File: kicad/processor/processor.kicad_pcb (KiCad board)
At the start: 4 copper layers, 75 x 50 mm, 95 parts, among them J101 CONN_02X07, J201 V_QI, J202 GND, J203 Battery, M401 MICROSD, Q201 DMG3415U, Q202 DMG3415U, Q203 DMG3414U, Q204 DMG3415U, Q205 DMG3415U, Q301 DMG3415U, Q401 DMG3415U, Q501 MMBT4401, Q502 MMBT4401, SW201 SW, SW501 SWITCH_PUSHBUTTON, SW502 SWITCH_PUSHBUTTON, U101 ESP32-WROOM, U102 BME280, U103 TCA9534A, U201 MCP73832, U202 NCP694-3.3, U301 FGPMMOPA6H, U501 USB_B_Socket, U502 SP3003-04, U503 CP2102N

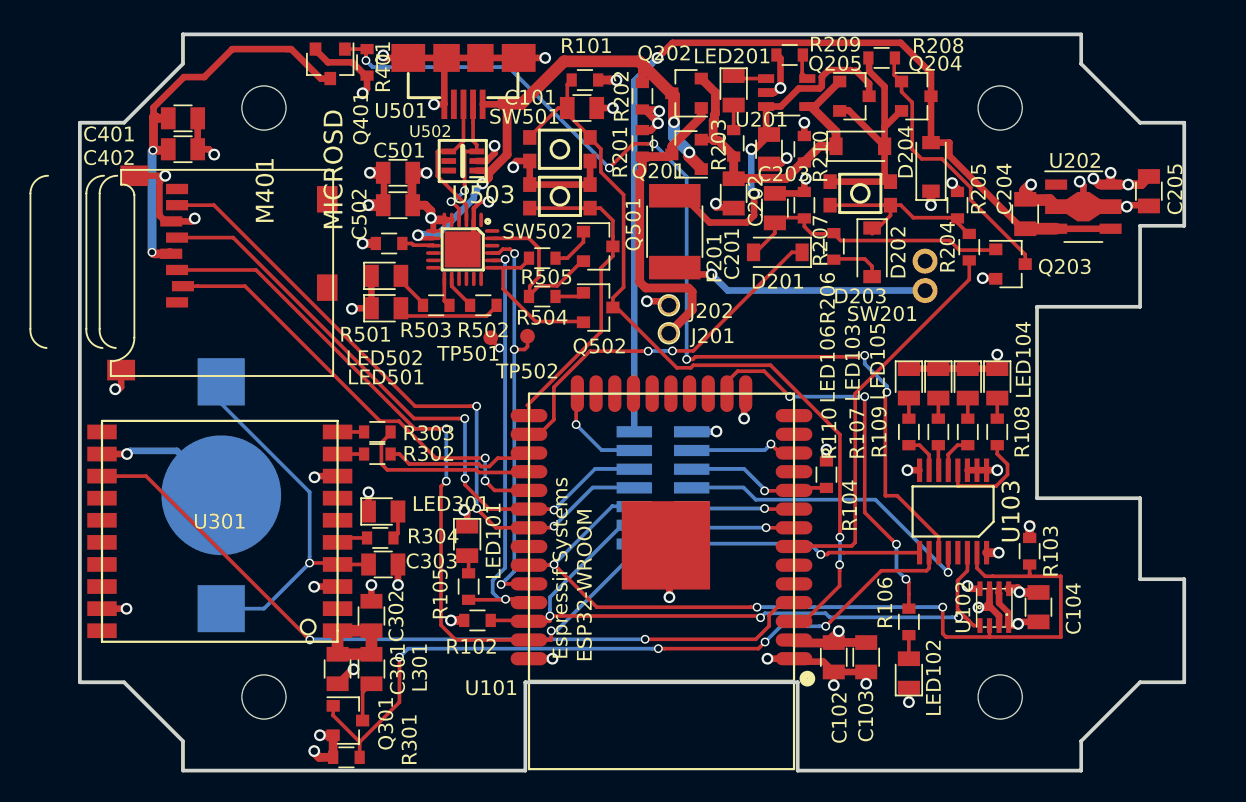
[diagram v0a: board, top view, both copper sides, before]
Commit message: Split analog SPI to be separate from SD pins, USB bus powered, added caps, updated todo, more
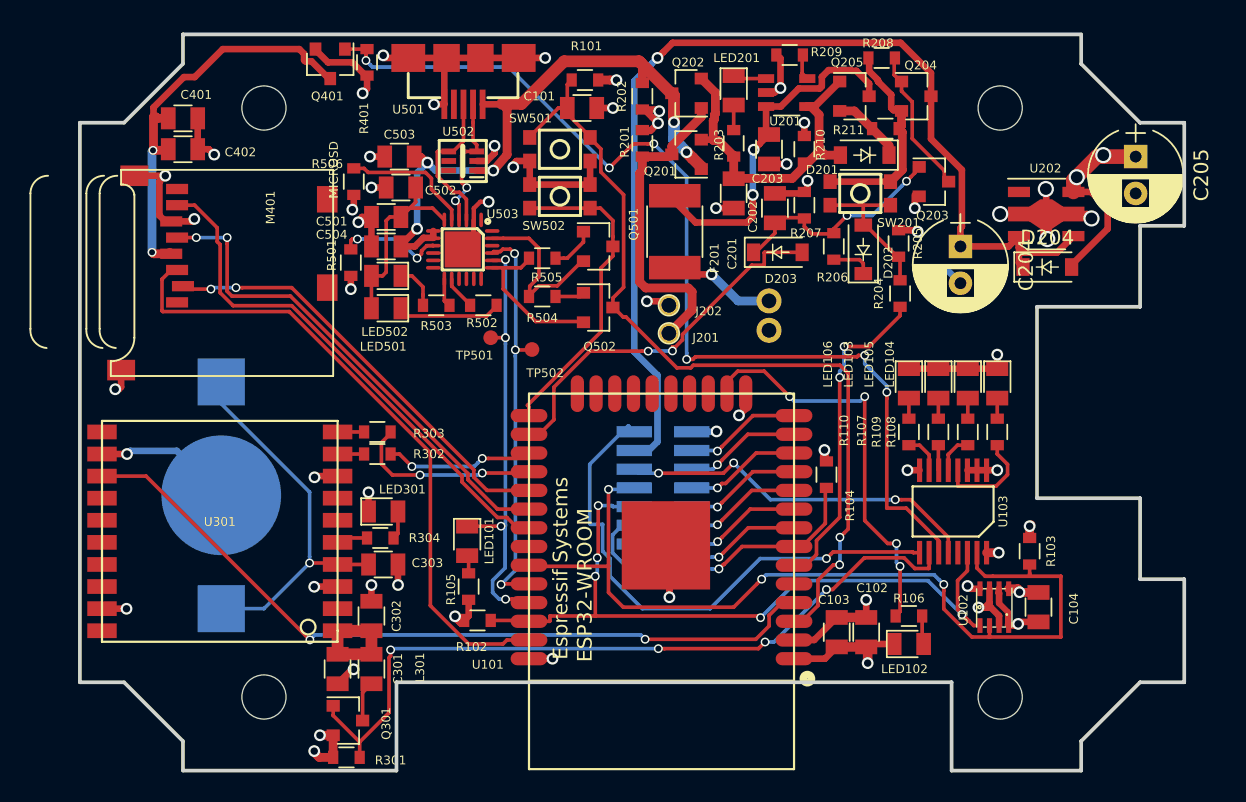
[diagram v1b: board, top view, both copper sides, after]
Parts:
- added C503: 4.7uF, paddle:SMD_0805, F.Cu at (21.7, 8.30)
- added C504: 0.1uF, paddle:SMD_0805, F.Cu at (20.8, 14.4)
- added R211: 1R0, paddle:R_0603, F.Cu at (54.7, 6.40)
- added R506: 1k, paddle:R_0603, F.Cu at (18.6, 10.0)
- C204, C205: value 10uF -> 100uF/10V; footprint paddle:SMD_0805 -> Capacitors_THT:CP_Radial_D6.3mm_P2.50mm
- C501: value 10uF -> 4.7uF
- D201, D203, D204: value SS24FL -> Schottky
- R107, R110: value 330 -> 220
- R205: value 1Meg -> 100k
- moved J203 10.9 mm to (46.8, 19.1), turned to 270 degrees
- moved D204 10.4 mm to (65.7, 15.8), turned to 0 degrees
- moved D203 9.12 mm to (47.4, 14.8)
- moved D201 8.85 mm to (53.3, 8.20)
- moved Q203 7.64 mm to (58.0, 10.0)
- moved R204 5.66 mm to (55.7, 17.6)
- moved C204 4.92 mm to (59.8, 14.4), turned to 270 degrees
- moved R205 4.77 mm to (55.6, 14.2)
- moved C501 3.10 mm to (20.8, 12.4)
- moved R501 2.91 mm to (18.4, 15.5), turned to 270 degrees
- moved C102 2.78 mm to (53.4, 40.6)
- moved C103 2.62 mm to (51.4, 40.6)
- moved U202 2.57 mm to (65.6, 12.2)
- moved C205 2.52 mm to (71.7, 8.30)
- moved LED102 2.00 mm to (56.3, 41.4), turned to 0 degrees
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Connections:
- C501 pad 1: +3V3 -> Net-(C501-Pad1)
- C502 pad 1: +3V3 -> Net-(C501-Pad1)
- D201 pad 1: /KEEPALIVE -> Net-(D201-Pad1)
- D201 pad 2: Net-(C202-Pad1) -> /power/V+EXT
- D203 pad 1: /power/V+EXT -> Net-(C202-Pad1)
- D203 pad 2: /power/V_UNREG -> /KEEPALIVE
- D204 pad 1: +3V3 -> /+V_UNREG_SW
- D204 pad 2: /+V_UNREG_SW -> +3V3
- J101 pad 1: /SPI_SDO -> /AN3_CS*
- J101 pad 10: /BUSY* -> /SPI_MISO
- J101 pad 11: /AN3_CS* -> /+V_UNREG_SW
- J101 pad 12: /AN0_CS* -> /SPI_SCLK
- J101 pad 13: /+V_UNREG_SW -> /+3.3VA_ENABLE
- J101 pad 2: /+3.3VA_ENABLE -> /AN2_CS*
- J101 pad 3: /I2C_SCK -> /PIO_B_BUSY*
- J101 pad 5: /I2C_SDA -> /I2C_SCK
- J101 pad 6: /AN2_CS* -> /AN0_CS*
- J101 pad 7: /SPI_SDI -> /I2C_SDA
- J101 pad 8: /AN_REFSEL -> /SPI_MOSI
- J101 pad 9: /SPI_SCLK -> /PIO_A
- LED101 pad 1: GND -> /CON_TXD
- LED501 pad 1: GND -> Net-(LED501-Pad1)
- LED501 pad 2: Net-(LED501-Pad2) -> Net-(C501-Pad1)
- LED502 pad 1: GND -> Net-(LED502-Pad1)
- LED502 pad 2: Net-(LED502-Pad2) -> Net-(C501-Pad1)
- M401 pad 1: Net-(M401-Pad1) -> (no net)
- M401 pad 3: /SPI_SDO -> /SD_MOSI
- M401 pad 5: /SPI_SCLK -> /SD_SCLK
- M401 pad 7: /SPI_SDI -> /SD_MISO
- M401 pad 8: Net-(M401-Pad8) -> (no net)
- M401 pad CD1: Net-(M401-PadCD1) -> (no net)
- M401 pad CD2: Net-(M401-PadCD2) -> (no net)
- Q205 pad 2: /power/V_UNREG -> Net-(D201-Pad1)
- R104 pad 2: /BUSY* -> /PIO_B_BUSY*
- R105 pad 1: /CON_TXD -> +3V3
- R204 pad 2: Net-(D202-Pad1) -> Net-(D202-Pad2)
- R205 pad 2: Net-(D202-Pad1) -> Net-(D202-Pad2)
- R206 pad 2: Net-(D202-Pad2) -> Net-(D202-Pad1)
- R502 pad 2: Net-(LED501-Pad2) -> Net-(LED501-Pad1)
- R503 pad 2: Net-(LED502-Pad2) -> Net-(LED502-Pad1)
- SW201 pad 1: Net-(D202-Pad1) -> Net-(D202-Pad2)
- U101 pad 10: /BUSY* -> /AN1_CS*
- U101 pad 11: Net-(U101-Pad11) -> /AN0_CS*
- U101 pad 12: /AN0_CS* -> /SPI_MOSI
- U101 pad 13: Net-(U101-Pad13) -> /SPI_MISO
- U101 pad 14: Net-(U101-Pad14) -> /SPI_SCLK
- U101 pad 17: Net-(U101-Pad17) -> (no net)
- U101 pad 18: Net-(U101-Pad18) -> (no net)
- U101 pad 19: Net-(U101-Pad19) -> (no net)
- U101 pad 20: Net-(U101-Pad20) -> (no net)
- U101 pad 21: Net-(U101-Pad21) -> (no net)
- U101 pad 22: Net-(U101-Pad22) -> (no net)
- U101 pad 23: Net-(U101-Pad23) -> (no net)
- U101 pad 24: /AN3_CS* -> (no net)
- U101 pad 30: /SPI_SCLK -> /SD_SCLK
- U101 pad 31: /SPI_SDI -> /SD_MISO
- U101 pad 32: Net-(U101-Pad32) -> (no net)
- U101 pad 37: /SPI_SDO -> /SD_MOSI
- U101 pad 5: Net-(U101-Pad5) -> (no net)
- U101 pad 6: Net-(U101-Pad6) -> /POWER_SW*
- U101 pad 7: /POWER_SW* -> /PIO_B_BUSY*
- U101 pad 8: /AN1_CS* -> /AN3_CS*
- U103 pad 12: /AN_REFSEL -> /PIO_A
- U103 pad 13: Net-(U103-Pad13) -> (no net)
- U202 pad 1: Net-(U202-Pad1) -> (no net)
- U301 pad 11: Net-(U301-Pad11) -> (no net)
- U301 pad 14: Net-(U301-Pad14) -> (no net)
- U301 pad 15: Net-(U301-Pad15) -> (no net)
- U301 pad 16: Net-(U301-Pad16) -> (no net)
- U301 pad 17: Net-(U301-Pad17) -> (no net)
- U301 pad 18: Net-(U301-Pad18) -> (no net)
- U301 pad 20: Net-(U301-Pad20) -> (no net)
- U501 pad 4: Net-(U501-Pad4) -> (no net)
- U502 pad 5: Net-(U502-Pad5) -> (no net)
- U502 pad 6: Net-(U502-Pad6) -> (no net)
- U503 pad 1: Net-(U503-Pad1) -> (no net)
- U503 pad 10: Net-(U503-Pad10) -> (no net)
- U503 pad 11: Net-(U503-Pad11) -> (no net)
- U503 pad 12: Net-(U503-Pad12) -> (no net)
- U503 pad 15: Net-(U503-Pad15) -> (no net)
- U503 pad 16: Net-(U503-Pad16) -> (no net)
- U503 pad 17: Net-(U503-Pad17) -> (no net)
- U503 pad 18: Net-(U503-Pad18) -> (no net)
- U503 pad 22: Net-(U503-Pad22) -> (no net)
- U503 pad 24: Net-(U503-Pad24) -> (no net)
- U503 pad 5: +3V3 -> Net-(R506-Pad2)
- U503 pad 6: +3V3 -> Net-(C501-Pad1)
- U503 pad 7: +3V3 -> /USB/+VBUS
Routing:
- net /SPI_SDO: track 53.2 -> 0.00 mm, vias 3 -> 0
- net /SPI_SDI: track 45.7 -> 0.00 mm, vias 3 -> 0
- net /SD_MOSI: track 0.00 -> 43.9 mm
- net /SD_MISO: track 0.00 -> 35.7 mm
- net /SPI_SCLK: track 42.5 -> 7.96 mm, vias 3 -> 1
- net /SD_SCLK: track 0.00 -> 33.9 mm, vias 0 -> 2
- net /PIO_A: track 0.00 -> 24.9 mm, vias 0 -> 3
- net /PIO_B_BUSY*: track 0.00 -> 21.6 mm, vias 0 -> 1
- net /AN_REFSEL: track 21.1 -> 0.00 mm, vias 1 -> 0
- net /+3.3VA_ENABLE: track 15.8 -> 36.5 mm
- net Net-(C501-Pad1): track 0.00 -> 13.9 mm
- net /power/V+BAT: track 17.6 -> 7.34 mm
- net Net-(D202-Pad1): track 13.1 -> 2.80 mm
- net /BUSY*: track 9.81 -> 0.00 mm, vias 1 -> 0
- net Net-(R506-Pad2): track 0.00 -> 8.94 mm
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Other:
- outline, holes or cut-outs redrawn

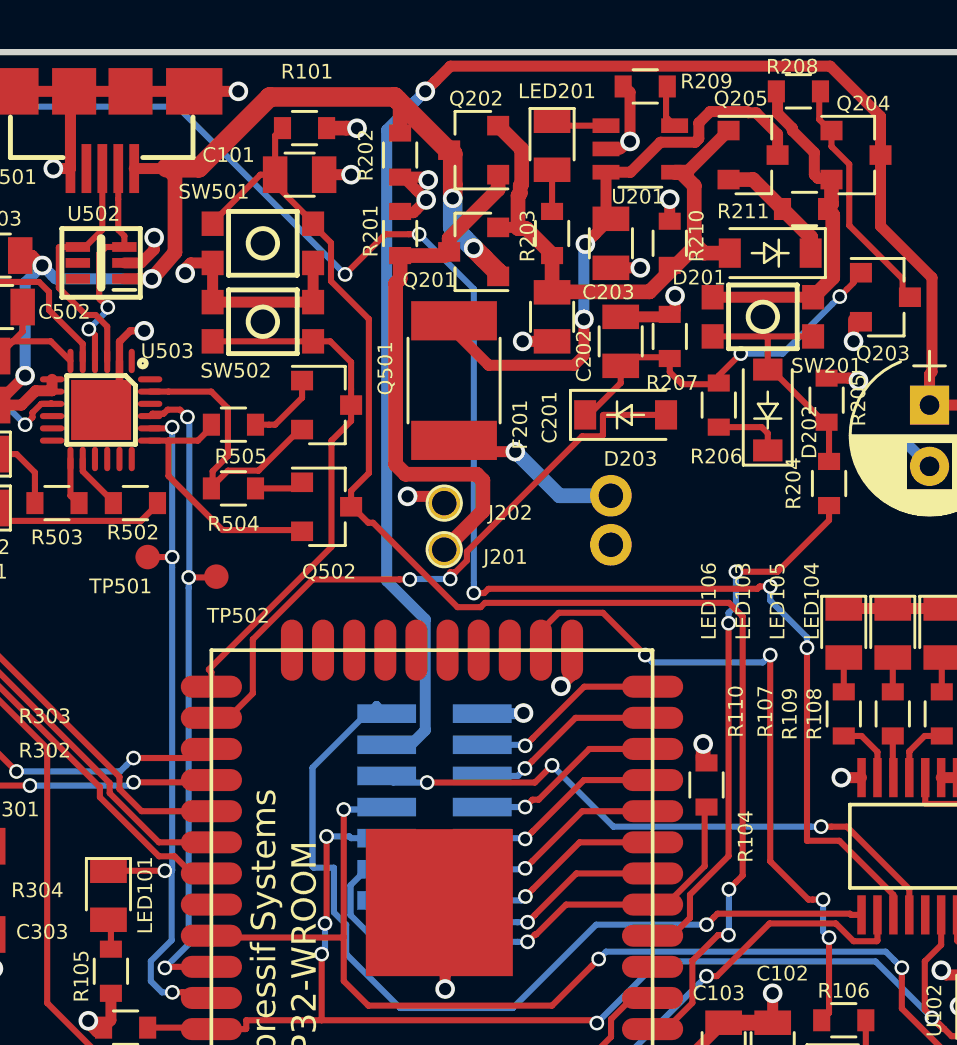
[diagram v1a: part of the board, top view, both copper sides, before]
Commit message: processor laid out, todo complete, connector for wireless charge
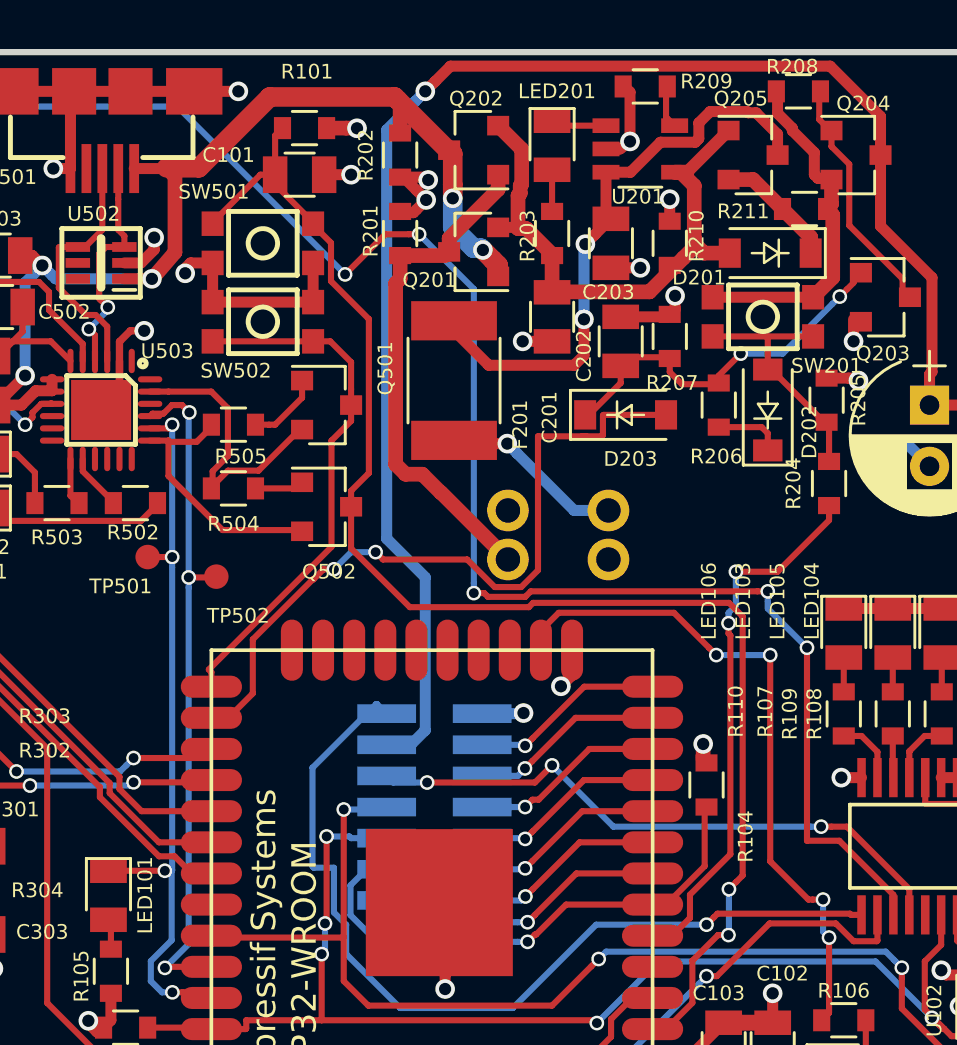
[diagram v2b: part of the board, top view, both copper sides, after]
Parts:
- removed J202: GND, paddle:TH_1.0
- D201, D203, D204: value Schottky -> SS24FL
- J101: value CONN_02X07 -> FCI 20021321-00014T4LF
- J201: value V_QI -> S2B-PH-K-S(LF)(SN); footprint paddle:TH_1.0 -> paddle:JST_battery_header_B2B-PH-K-S; moved to B.Cu
- J203: value Battery -> S2B-PH-K-S(LF)(SN)
- moved J201 2.67 mm to (42.6, 19.7), turned to 90 degrees
- moved J203 0.61 mm to (46.7, 19.7)
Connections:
- M401 pad 1: (no net) -> Net-(M401-Pad1)
- M401 pad 8: (no net) -> Net-(M401-Pad8)
- M401 pad CD1: (no net) -> Net-(M401-PadCD1)
- M401 pad CD2: (no net) -> Net-(M401-PadCD2)
- U101 pad 17: (no net) -> Net-(U101-Pad17)
- U101 pad 18: (no net) -> Net-(U101-Pad18)
- U101 pad 19: (no net) -> Net-(U101-Pad19)
- U101 pad 20: (no net) -> Net-(U101-Pad20)
- U101 pad 21: (no net) -> Net-(U101-Pad21)
- U101 pad 22: (no net) -> Net-(U101-Pad22)
- U101 pad 23: (no net) -> Net-(U101-Pad23)
- U101 pad 24: (no net) -> Net-(U101-Pad24)
- U101 pad 32: (no net) -> Net-(U101-Pad32)
- U101 pad 5: (no net) -> Net-(U101-Pad5)
- U103 pad 13: (no net) -> Net-(U103-Pad13)
- U202 pad 1: (no net) -> Net-(U202-Pad1)
- U301 pad 11: (no net) -> Net-(U301-Pad11)
- U301 pad 14: (no net) -> Net-(U301-Pad14)
- U301 pad 15: (no net) -> Net-(U301-Pad15)
- U301 pad 16: (no net) -> Net-(U301-Pad16)
- U301 pad 17: (no net) -> Net-(U301-Pad17)
- U301 pad 18: (no net) -> Net-(U301-Pad18)
- U301 pad 20: (no net) -> Net-(U301-Pad20)
- U501 pad 4: (no net) -> Net-(U501-Pad4)
- U502 pad 5: (no net) -> Net-(U502-Pad5)
- U502 pad 6: (no net) -> Net-(U502-Pad6)
- U503 pad 1: (no net) -> Net-(U503-Pad1)
- U503 pad 10: (no net) -> Net-(U503-Pad10)
- U503 pad 11: (no net) -> Net-(U503-Pad11)
- U503 pad 12: (no net) -> Net-(U503-Pad12)
- U503 pad 15: (no net) -> Net-(U503-Pad15)
- U503 pad 16: (no net) -> Net-(U503-Pad16)
- U503 pad 17: (no net) -> Net-(U503-Pad17)
- U503 pad 18: (no net) -> Net-(U503-Pad18)
- U503 pad 22: (no net) -> Net-(U503-Pad22)
- U503 pad 24: (no net) -> Net-(U503-Pad24)
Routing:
- net /KEEPALIVE: track 25.9 -> 30.1 mm
- net GND: track 129.9 -> 128.3 mm, vias 46 -> 45
- net Net-(J201-Pad1): track 22.0 -> 20.9 mm
- net /RESET_ESP*: track 57.9 -> 58.9 mm
- net /power/V+EXT: track 23.7 -> 24.4 mm

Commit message: Analog board and second rev processor board as sent to Goldphoenix
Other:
- outline, holes or cut-outs redrawn
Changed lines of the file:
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@@
     (visible_elements 7FFDFFFF)
     (pcbplotparams
-      (layerselection 0x010e0_ffffffff)
+      (layerselection 0x010e8_ffffffff)
       (usegerberextensions true)
       (usegerberattributes false)
@@
   (gr_line (start 0 -0.3) (end 0 0.3) (layer Dwgs.User) (width 0.2))
   (gr_line (start 21.5 50) (end 7 50) (layer Edge.Cuts) (width 0.25))
-  (gr_line (start 59.2 50) (end 68 50) (layer Edge.Cuts) (width 0.25))
-  (gr_line (start 59.2 44) (end 59.2 50) (layer Edge.Cuts) (width 0.25))
-  (gr_line (start 21.5 44) (end 59.2 44) (layer Edge.Cuts) (width 0.25))
+  (gr_line (start 58.5 50) (end 68 50) (layer Edge.Cuts) (width 0.25))
+  (gr_line (start 58.5 44) (end 58.5 50) (layer Edge.Cuts) (width 0.25))
+  (gr_line (start 21.5 44) (end 58.5 44) (layer Edge.Cuts) (width 0.25))
   (gr_line (start 21.5 50) (end 21.5 44) (layer Edge.Cuts) (width 0.25))
   (gr_line (start 68 2) (end 72 6) (angle 90) (layer Edge.Cuts) (width 0.25))
